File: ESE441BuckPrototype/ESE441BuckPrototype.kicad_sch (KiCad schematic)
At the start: 0 parts

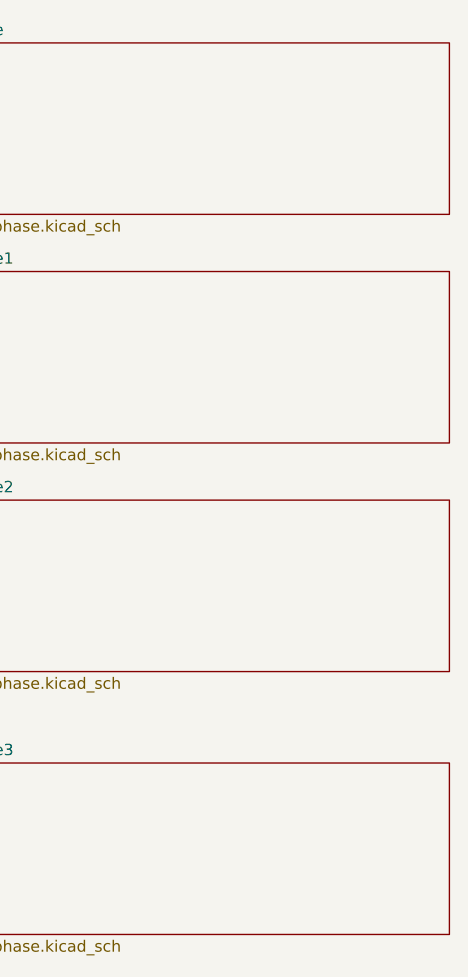
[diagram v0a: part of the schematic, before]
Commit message: Add SIC645 half H-bridge
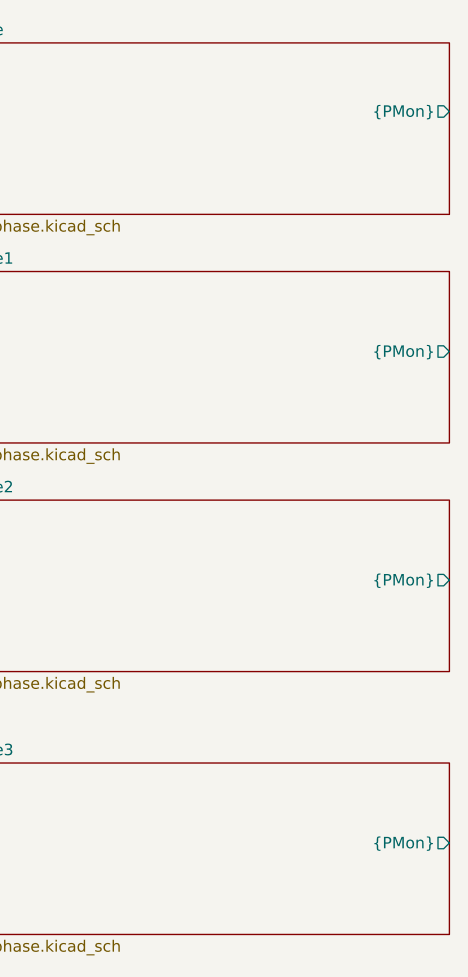
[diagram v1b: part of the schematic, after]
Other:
- sheet Single_Phase ports: added {PMon}; removed none
- sheet Single_Phase1 ports: added {PMon}; removed none
- sheet Single_Phase2 ports: added {PMon}; removed none
- sheet Single_Phase3 ports: added {PMon}; removed none

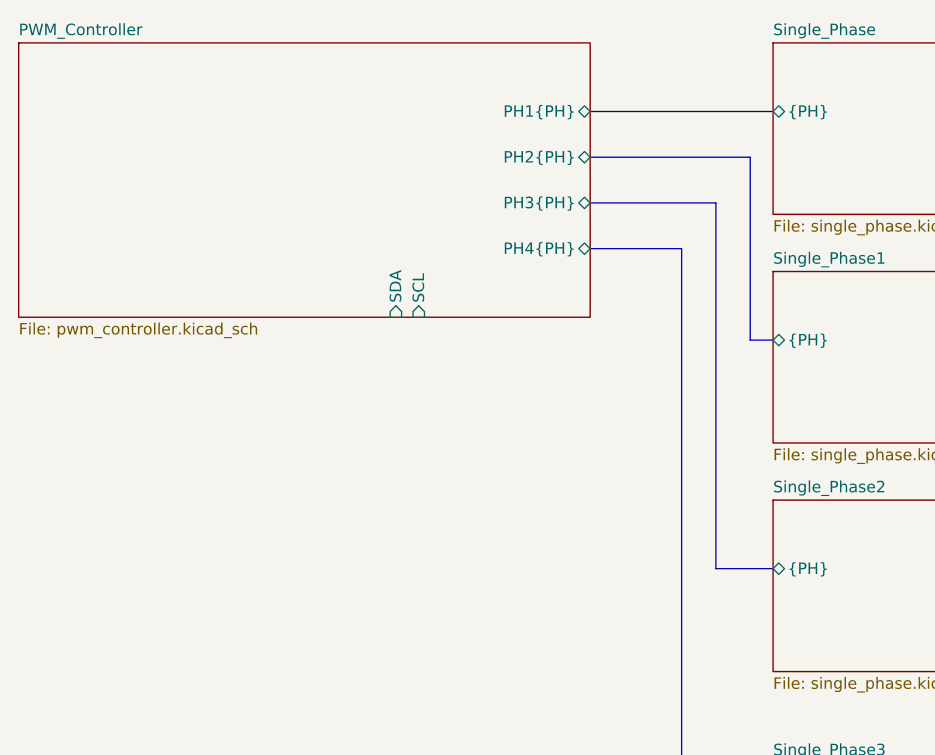
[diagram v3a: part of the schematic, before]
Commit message: Change I2C to bus
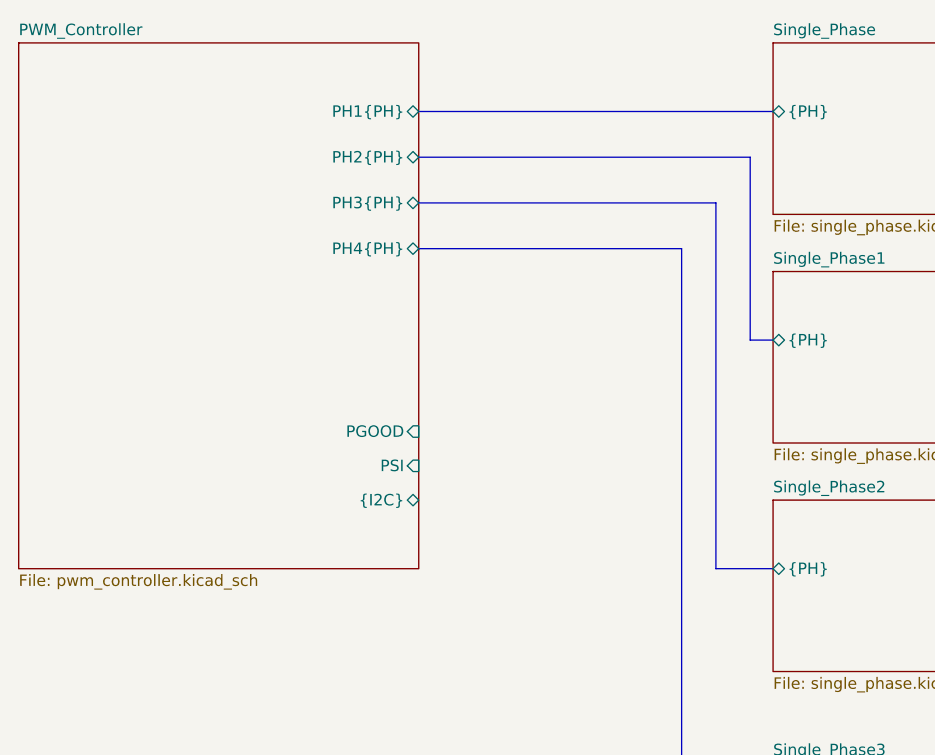
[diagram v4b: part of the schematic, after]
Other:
- sheet PWM_Controller ports: added PGOOD, PSI, {I2C}; removed SCL, SDA
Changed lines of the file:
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@@
     (stroke (width 0) (type default) (color 0 0 0 0))
   )
-  (bus (pts (xy 99.06 57.15) (xy 109.22 57.15))
-    (stroke (width 0) (type default) (color 0 0 0 0))
-  )
-  (bus (pts (xy 99.06 46.99) (xy 116.84 46.99))
-    (stroke (width 0) (type default) (color 0 0 0 0))
-  )
-  (bus (pts (xy 99.06 52.07) (xy 113.03 52.07))
+  (bus (pts (xy 80.01 57.15) (xy 109.22 57.15))
+    (stroke (width 0) (type default) (color 0 0 0 0))
+  )
+  (bus (pts (xy 80.01 46.99) (xy 116.84 46.99))
+    (stroke (width 0) (type default) (color 0 0 0 0))
+  )
+  (bus (pts (xy 80.01 52.07) (xy 113.03 52.07))
     (stroke (width 0) (type default) (color 0 0 0 0))
   )
@@
     (stroke (width 0) (type default) (color 0 0 0 0))
   )
-  (bus (pts (xy 99.06 41.91) (xy 119.38 41.91))
+  (bus (pts (xy 80.01 41.91) (xy 119.38 41.91))
     (stroke (width 0) (type default) (color 0 0 0 0))
   )
@@
     )
   )
-  (sheet (at 35.56 34.29) (size 63.5 30.48) (fields_autoplaced)
+  (sheet (at 35.56 34.29) (size 44.45 58.42) (fields_autoplaced)
     (stroke (width 0.1524) (type solid) (color 0 0 0 0))
     (fill (color 0 0 0 0.0000))
@@
       (effects (font (size 1.27 1.27)) (justify left bottom))
     )
-    (property "Sheet file" "pwm_controller.kicad_sch" (id 1) (at 35.56 65.3546 0)
-      (effects (font (size 1.27 1.27)) (justify left top))
-    )
-    (pin "SDA" input (at 77.47 64.77 270)
-      (effects (font (size 1.27 1.27)) (justify left))
-    )
-    (pin "SCL" input (at 80.01 64.77 270)
-      (effects (font (size 1.27 1.27)) (justify left))
-    )
-    (pin "PH4{PH}" bidirectional (at 99.06 57.15 0)
-      (effects (font (size 1.27 1.27)) (justify right))
-    )
-    (pin "PH3{PH}" bidirectional (at 99.06 52.07 0)
-      (effects (font (size 1.27 1.27)) (justify right))
-    )
-    (pin "PH1{PH}" bidirectional (at 99.06 41.91 0)
-      (effects (font (size 1.27 1.27)) (justify right))
-    )
-    (pin "PH2{PH}" bidirectional (at 99.06 46.99 0)
+    (property "Sheet file" "pwm_controller.kicad_sch" (id 1) (at 35.56 93.2946 0)
+      (effects (font (size 1.27 1.27)) (justify left top))
+    )
+    (pin "PH4{PH}" bidirectional (at 80.01 57.15 0)
+      (effects (font (size 1.27 1.27)) (justify right))
+    )
+    (pin "PH3{PH}" bidirectional (at 80.01 52.07 0)
+      (effects (font (size 1.27 1.27)) (justify right))
+    )
+    (pin "PH1{PH}" bidirectional (at 80.01 41.91 0)
+      (effects (font (size 1.27 1.27)) (justify right))
+    )
+    (pin "PH2{PH}" bidirectional (at 80.01 46.99 0)
+      (effects (font (size 1.27 1.27)) (justify right))
+    )
+    (pin "PSI" input (at 80.01 81.28 0)
+      (effects (font (size 1.27 1.27)) (justify right))
+    )
+    (pin "PGOOD" input (at 80.01 77.47 0)
+      (effects (font (size 1.27 1.27)) (justify right))
+    )
+    (pin "{I2C}" bidirectional (at 80.01 85.09 0)
       (effects (font (size 1.27 1.27)) (justify right))
     )
@@
       (reference "#PWR?") (unit 1) (value "+1V0") (footprint "")
     )
+    (path "/c40b8f97-aa7c-4f3d-8800-858f1175d449/47b0d83e-953e-4c79-b379-6d6a841fd174"
+      (reference "#PWR?") (unit 1) (value "GND") (footprint "")
+    )
+    (path "/3ec646dd-5f40-4b1c-a84e-9994d2a2ab3f/47b0d83e-953e-4c79-b379-6d6a841fd174"
+      (reference "#PWR?") (unit 1) (value "GND") (footprint "")
+    )
+    (path "/6a18841e-10d2-462e-9013-c46f018cb15d/47b0d83e-953e-4c79-b379-6d6a841fd174"
+      (reference "#PWR?") (unit 1) (value "GND") (footprint "")
+    )
     (path "/3fb02998-24e2-415c-be56-4aa08d7c33e1/47b0d83e-953e-4c79-b379-6d6a841fd174"
-      (reference "#PWR?") (unit 1) (value "GND") (footprint "")
-    )
-    (path "/3ec646dd-5f40-4b1c-a84e-9994d2a2ab3f/47b0d83e-953e-4c79-b379-6d6a841fd174"
-      (reference "#PWR?") (unit 1) (value "GND") (footprint "")
-    )
-    (path "/c40b8f97-aa7c-4f3d-8800-858f1175d449/47b0d83e-953e-4c79-b379-6d6a841fd174"
-      (reference "#PWR?") (unit 1) (value "GND") (footprint "")
-    )
-    (path "/6a18841e-10d2-462e-9013-c46f018cb15d/47b0d83e-953e-4c79-b379-6d6a841fd174"
       (reference "#PWR?") (unit 1) (value "GND") (footprint "")
     )
@@
       (reference "#PWR?") (unit 1) (value "+3V3") (footprint "")
     )
+    (path "/c40b8f97-aa7c-4f3d-8800-858f1175d449/aa70deba-9c9d-41d3-b0ab-228682a521a0"
+      (reference "#PWR?") (unit 1) (value "+5V") (footprint "")
+    )
+    (path "/3ec646dd-5f40-4b1c-a84e-9994d2a2ab3f/aa70deba-9c9d-41d3-b0ab-228682a521a0"
+      (reference "#PWR?") (unit 1) (value "+5V") (footprint "")
+    )
     (path "/6a18841e-10d2-462e-9013-c46f018cb15d/aa70deba-9c9d-41d3-b0ab-228682a521a0"
       (reference "#PWR?") (unit 1) (value "+5V") (footprint "")
     )
     (path "/3fb02998-24e2-415c-be56-4aa08d7c33e1/aa70deba-9c9d-41d3-b0ab-228682a521a0"
-      (reference "#PWR?") (unit 1) (value "+5V") (footprint "")
-    )
-    (path "/3ec646dd-5f40-4b1c-a84e-9994d2a2ab3f/aa70deba-9c9d-41d3-b0ab-228682a521a0"
-      (reference "#PWR?") (unit 1) (value "+5V") (footprint "")
-    )
-    (path "/c40b8f97-aa7c-4f3d-8800-858f1175d449/aa70deba-9c9d-41d3-b0ab-228682a521a0"
       (reference "#PWR?") (unit 1) (value "+5V") (footprint "")
     )
@@
       (reference "#PWR?") (unit 1) (value "VIN") (footprint "")
     )
+    (path "/3ec646dd-5f40-4b1c-a84e-9994d2a2ab3f/c609dea9-46c5-4f5b-9e33-3279001ef329"
+      (reference "#PWR?") (unit 1) (value "GNDPWR") (footprint "")
+    )
+    (path "/c40b8f97-aa7c-4f3d-8800-858f1175d449/c609dea9-46c5-4f5b-9e33-3279001ef329"
+      (reference "#PWR?") (unit 1) (value "GNDPWR") (footprint "")
+    )
     (path "/3fb02998-24e2-415c-be56-4aa08d7c33e1/c609dea9-46c5-4f5b-9e33-3279001ef329"
       (reference "#PWR?") (unit 1) (value "GNDPWR") (footprint "")
     )
-    (path "/c40b8f97-aa7c-4f3d-8800-858f1175d449/c609dea9-46c5-4f5b-9e33-3279001ef329"
-      (reference "#PWR?") (unit 1) (value "GNDPWR") (footprint "")
-    )
     (path "/6a18841e-10d2-462e-9013-c46f018cb15d/c609dea9-46c5-4f5b-9e33-3279001ef329"
-      (reference "#PWR?") (unit 1) (value "GNDPWR") (footprint "")
-    )
-    (path "/3ec646dd-5f40-4b1c-a84e-9994d2a2ab3f/c609dea9-46c5-4f5b-9e33-3279001ef329"
       (reference "#PWR?") (unit 1) (value "GNDPWR") (footprint "")
     )
@@
       (reference "C4") (unit 1) (value "1u") (footprint "")
     )
+    (path "/c40b8f97-aa7c-4f3d-8800-858f1175d449/0b979782-7fb6-42d5-9003-f3031e17e259"
+      (reference "C?") (unit 1) (value "C_Small") (footprint "Capacitor_SMD:C_0603_1608Metric")
+    )
+    (path "/6a18841e-10d2-462e-9013-c46f018cb15d/0b979782-7fb6-42d5-9003-f3031e17e259"
+      (reference "C?") (unit 1) (value "C_Small") (footprint "Capacitor_SMD:C_0603_1608Metric")
+    )
     (path "/3fb02998-24e2-415c-be56-4aa08d7c33e1/0b979782-7fb6-42d5-9003-f3031e17e259"
-      (reference "C?") (unit 1) (value "C_Small") (footprint "Capacitor_SMD:C_0603_1608Metric")
-    )
-    (path "/6a18841e-10d2-462e-9013-c46f018cb15d/0b979782-7fb6-42d5-9003-f3031e17e259"
-      (reference "C?") (unit 1) (value "C_Small") (footprint "Capacitor_SMD:C_0603_1608Metric")
-    )
-    (path "/c40b8f97-aa7c-4f3d-8800-858f1175d449/0b979782-7fb6-42d5-9003-f3031e17e259"
       (reference "C?") (unit 1) (value "C_Small") (footprint "Capacitor_SMD:C_0603_1608Metric")
     )
@@
       (reference "C?") (unit 1) (value "10n") (footprint "")
     )
+    (path "/6a18841e-10d2-462e-9013-c46f018cb15d/96576bda-09ba-4603-9b8a-5f995f488644"
+      (reference "C?") (unit 1) (value "C_Small") (footprint "Capacitor_SMD:C_0603_1608Metric")
+    )
     (path "/c40b8f97-aa7c-4f3d-8800-858f1175d449/96576bda-09ba-4603-9b8a-5f995f488644"
-      (reference "C?") (unit 1) (value "C_Small") (footprint "Capacitor_SMD:C_0603_1608Metric")
-    )
-    (path "/6a18841e-10d2-462e-9013-c46f018cb15d/96576bda-09ba-4603-9b8a-5f995f488644"
       (reference "C?") (unit 1) (value "C_Small") (footprint "Capacitor_SMD:C_0603_1608Metric")
     )
@@
       (reference "C?") (unit 1) (value "1u") (footprint "")
     )
+    (path "/3ec646dd-5f40-4b1c-a84e-9994d2a2ab3f/a3289061-ef6e-4686-bfc0-3270404eeaa2"
+      (reference "C?") (unit 1) (value "47n") (footprint "Capacitor_SMD:C_0603_1608Metric")
+    )
+    (path "/3fb02998-24e2-415c-be56-4aa08d7c33e1/a3289061-ef6e-4686-bfc0-3270404eeaa2"
+      (reference "C?") (unit 1) (value "47n") (footprint "Capacitor_SMD:C_0603_1608Metric")
+    )
     (path "/c40b8f97-aa7c-4f3d-8800-858f1175d449/a3289061-ef6e-4686-bfc0-3270404eeaa2"
       (reference "C?") (unit 1) (value "47n") (footprint "Capacitor_SMD:C_0603_1608Metric")
     )
-    (path "/3fb02998-24e2-415c-be56-4aa08d7c33e1/a3289061-ef6e-4686-bfc0-3270404eeaa2"
-      (reference "C?") (unit 1) (value "47n") (footprint "Capacitor_SMD:C_0603_1608Metric")
-    )
-    (path "/3ec646dd-5f40-4b1c-a84e-9994d2a2ab3f/a3289061-ef6e-4686-bfc0-3270404eeaa2"
-      (reference "C?") (unit 1) (value "47n") (footprint "Capacitor_SMD:C_0603_1608Metric")
-    )

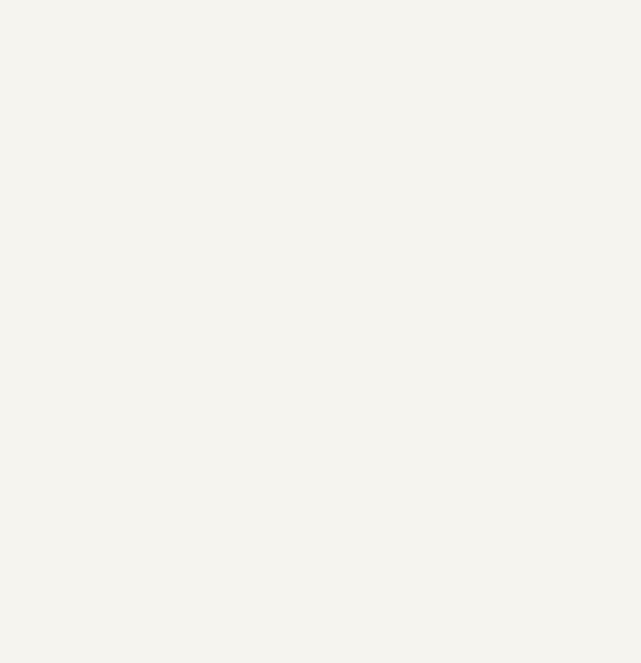
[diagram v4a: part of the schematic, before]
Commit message: Add ATMega1284p microcontroller for monitoring and voltage control
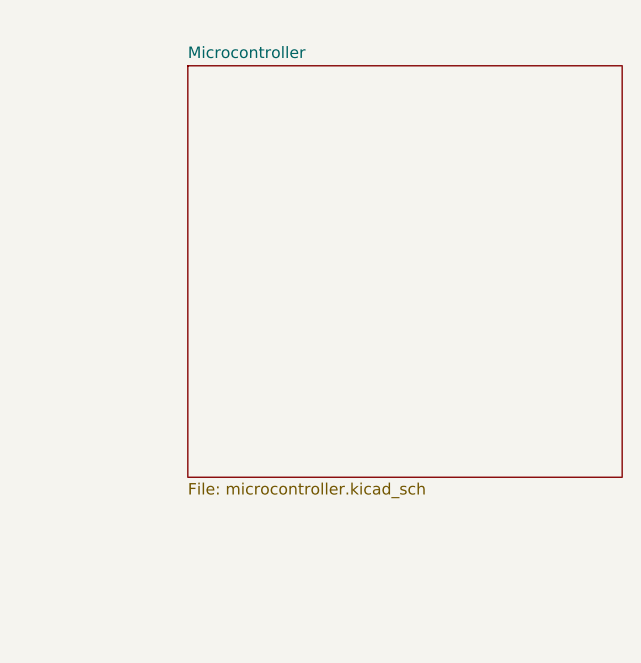
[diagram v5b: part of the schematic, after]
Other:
- added sheet Microcontroller (microcontroller.kicad_sch)
